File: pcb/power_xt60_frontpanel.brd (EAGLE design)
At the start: 86 x 31 mm, 21 parts, among them X1 SOLDERPAD4X5, X10 SOLDERPAD4X5, X11 SOLDERPAD4X5, X12 SOLDERPAD4X5, X2 SOLDERPAD4X5, X3 SOLDERPAD4X5, X4 SOLDERPAD4X5, X5 SOLDERPAD4X5, X6 SOLDERPAD4X5, X7 SOLDERPAD4X5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

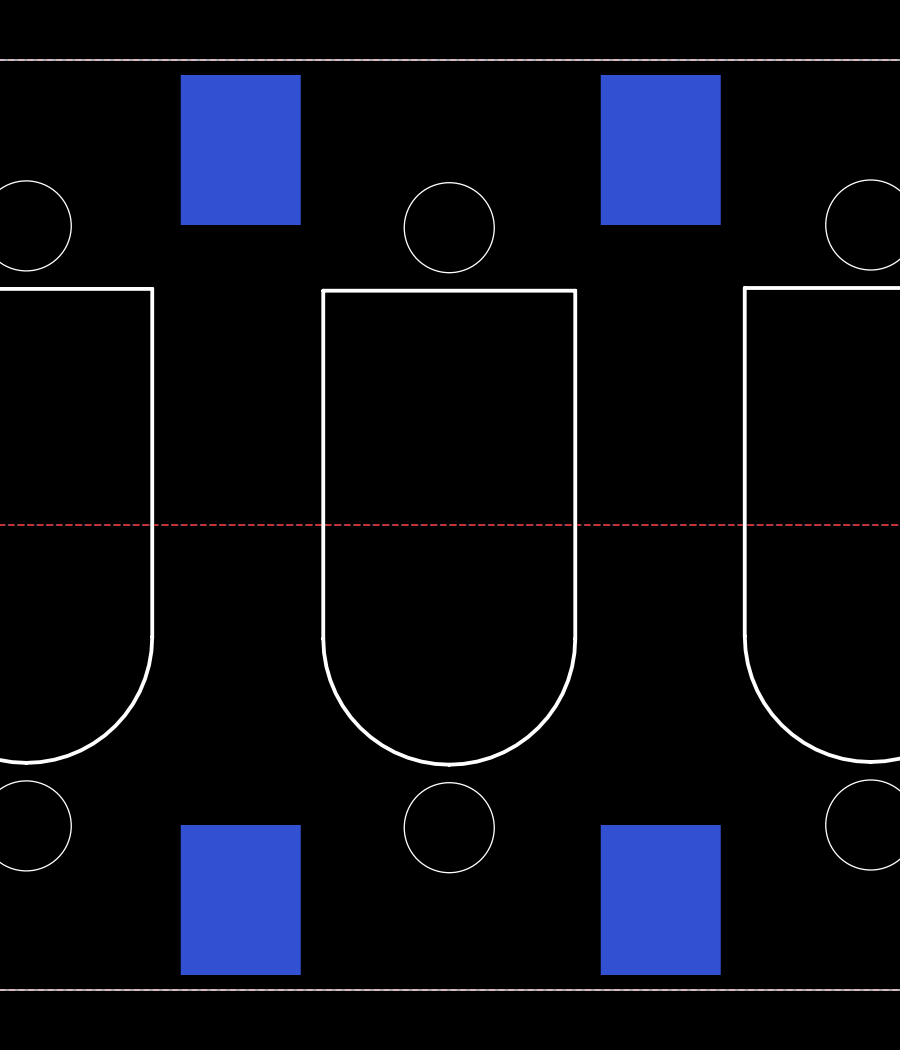
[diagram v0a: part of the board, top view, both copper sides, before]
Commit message: Fix alignment
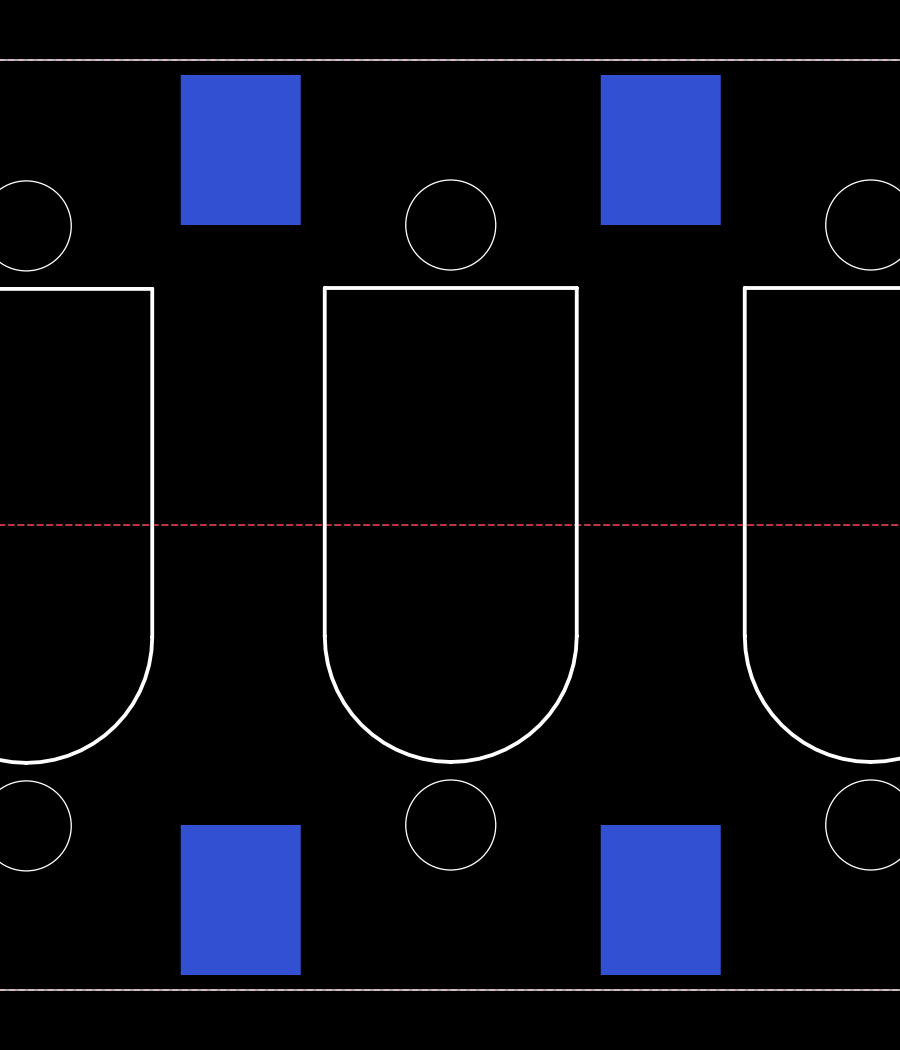
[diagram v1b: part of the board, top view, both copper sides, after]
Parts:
- moved H5 0.10 mm to (57.0, 15.5)
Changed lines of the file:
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@@
 <drawing>
 <settings>
-<setting alwaysvectorfont="yes"/>
+<setting alwaysvectorfont="no"/>
 <setting verticaltext="up"/>
 </settings>
@@
 <element name="H3" library="M2M-Holes" package="XT60E1-M-PANEL-HOLE" value="XT60E1-M-PANEL-HOLE" x="71" y="15.5" smashed="yes"/>
 <element name="H4" library="M2M-Holes" package="XT60E1-M-PANEL-HOLE" value="XT60E1-M-PANEL-HOLE" x="42.85" y="15.47" smashed="yes"/>
-<element name="H5" library="M2M-Holes" package="XT60E1-M-PANEL-HOLE" value="XT60E1-M-PANEL-HOLE" x="56.95" y="15.41" smashed="yes"/>
+<element name="H5" library="M2M-Holes" package="XT60E1-M-PANEL-HOLE" value="XT60E1-M-PANEL-HOLE" x="57" y="15.5" smashed="yes"/>
 <element name="H6" library="M2M-Holes" package="3.2-PAD" value="MOUNTHOLE-PAD3.2" x="82" y="4" smashed="yes"/>
 <element name="H7" library="M2M-Holes" package="3.2-PAD" value="MOUNTHOLE-PAD3.2" x="4" y="4" smashed="yes"/>

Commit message: Revison 2
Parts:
- moved H4 0.31 mm to (43.1, 15.5), turned to 180 degrees
- turned H1 to 180 degrees
- turned H2 to 180 degrees
- turned H3 to 180 degrees
- turned H5 to 180 degrees
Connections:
- net GND: now also H1.-, H2.-, H3.-, H4.-, H5.-
- net VCC: now also H1.+, H2.+, H3.+, H4.+, H5.+
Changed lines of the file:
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@@
 </autorouter>
 <elements>
-<element name="H1" library="M2M-Holes" package="XT60E1-M-PANEL-HOLE" value="XT60E1-M-PANEL-HOLE" x="15" y="15.5" smashed="yes"/>
-<element name="H2" library="M2M-Holes" package="XT60E1-M-PANEL-HOLE" value="XT60E1-M-PANEL-HOLE" x="29" y="15.5" smashed="yes"/>
-<element name="H3" library="M2M-Holes" package="XT60E1-M-PANEL-HOLE" value="XT60E1-M-PANEL-HOLE" x="71" y="15.5" smashed="yes"/>
-<element name="H4" library="M2M-Holes" package="XT60E1-M-PANEL-HOLE" value="XT60E1-M-PANEL-HOLE" x="42.85" y="15.47" smashed="yes"/>
-<element name="H5" library="M2M-Holes" package="XT60E1-M-PANEL-HOLE" value="XT60E1-M-PANEL-HOLE" x="57" y="15.5" smashed="yes"/>
+<element name="H1" library="M2M-Holes" package="XT60E1-M-PANEL-HOLE" value="XT60E1-M-PANEL-HOLE" x="15" y="15.5" smashed="yes" rot="R180"/>
+<element name="H2" library="M2M-Holes" package="XT60E1-M-PANEL-HOLE" value="XT60E1-M-PANEL-HOLE" x="29" y="15.5" smashed="yes" rot="R180"/>
+<element name="H3" library="M2M-Holes" package="XT60E1-M-PANEL-HOLE" value="XT60E1-M-PANEL-HOLE" x="71" y="15.5" smashed="yes" rot="R180"/>
+<element name="H4" library="M2M-Holes" package="XT60E1-M-PANEL-HOLE" value="XT60E1-M-PANEL-HOLE" x="43.15" y="15.53" smashed="yes" rot="R180"/>
+<element name="H5" library="M2M-Holes" package="XT60E1-M-PANEL-HOLE" value="XT60E1-M-PANEL-HOLE" x="57" y="15.5" smashed="yes" rot="R180"/>
 <element name="H6" library="M2M-Holes" package="3.2-PAD" value="MOUNTHOLE-PAD3.2" x="82" y="4" smashed="yes"/>
 <element name="H7" library="M2M-Holes" package="3.2-PAD" value="MOUNTHOLE-PAD3.2" x="4" y="4" smashed="yes"/>
@@
 <contactref element="X2" pad="1"/>
 <contactref element="X3" pad="1"/>
-<polygon width="0.1524" layer="16">
-<vertex x="0" y="15.5"/>
-<vertex x="86" y="15.5"/>
+<polygon width="1.016" layer="16">
+<vertex x="0" y="15"/>
+<vertex x="86" y="15"/>
 <vertex x="86" y="0"/>
 <vertex x="0" y="0"/>
@@
 <contactref element="H7" pad="B3,2"/>
 <contactref element="H6" pad="B3,2"/>
-<polygon width="0.1524" layer="1">
-<vertex x="0" y="15.5"/>
-<vertex x="86" y="15.5"/>
+<polygon width="1.016" layer="1">
+<vertex x="0" y="15"/>
+<vertex x="86" y="15"/>
 <vertex x="86" y="0"/>
 <vertex x="0" y="0"/>
 </polygon>
+<contactref element="H5" pad="+"/>
+<contactref element="H4" pad="+"/>
+<contactref element="H3" pad="+"/>
+<contactref element="H2" pad="+"/>
+<contactref element="H1" pad="+"/>
 </signal>
 <signal name="GND">
@@
 <contactref element="X5" pad="1"/>
 <contactref element="X4" pad="1"/>
-<polygon width="0.1524" layer="16" rank="2">
+<polygon width="1.016" layer="16" rank="2">
 <vertex x="0" y="31"/>
-<vertex x="0" y="15.5"/>
-<vertex x="86" y="15.5"/>
+<vertex x="0" y="16"/>
+<vertex x="86" y="16"/>
 <vertex x="86" y="31"/>
 </polygon>
@@
 <contactref element="H9" pad="B3,2"/>
 <contactref element="H8" pad="B3,2"/>
-<polygon width="0.1524" layer="1" rank="2">
+<polygon width="1.016" layer="1" rank="2">
 <vertex x="0" y="31"/>
 <vertex x="86" y="31"/>
-<vertex x="86" y="15.5"/>
-<vertex x="0" y="15.5"/>
+<vertex x="86" y="16"/>
+<vertex x="0" y="16"/>
 </polygon>
+<contactref element="H5" pad="-"/>
+<contactref element="H4" pad="-"/>
+<contactref element="H3" pad="-"/>
+<contactref element="H2" pad="-"/>
+<contactref element="H1" pad="-"/>
 </signal>
 </signals>
